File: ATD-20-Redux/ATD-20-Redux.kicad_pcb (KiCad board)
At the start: 2 copper layers, 17.8 x 57 mm, 5 parts, among them J1 RTC Pins, U1 DS1315, Y1 32.768 KHz

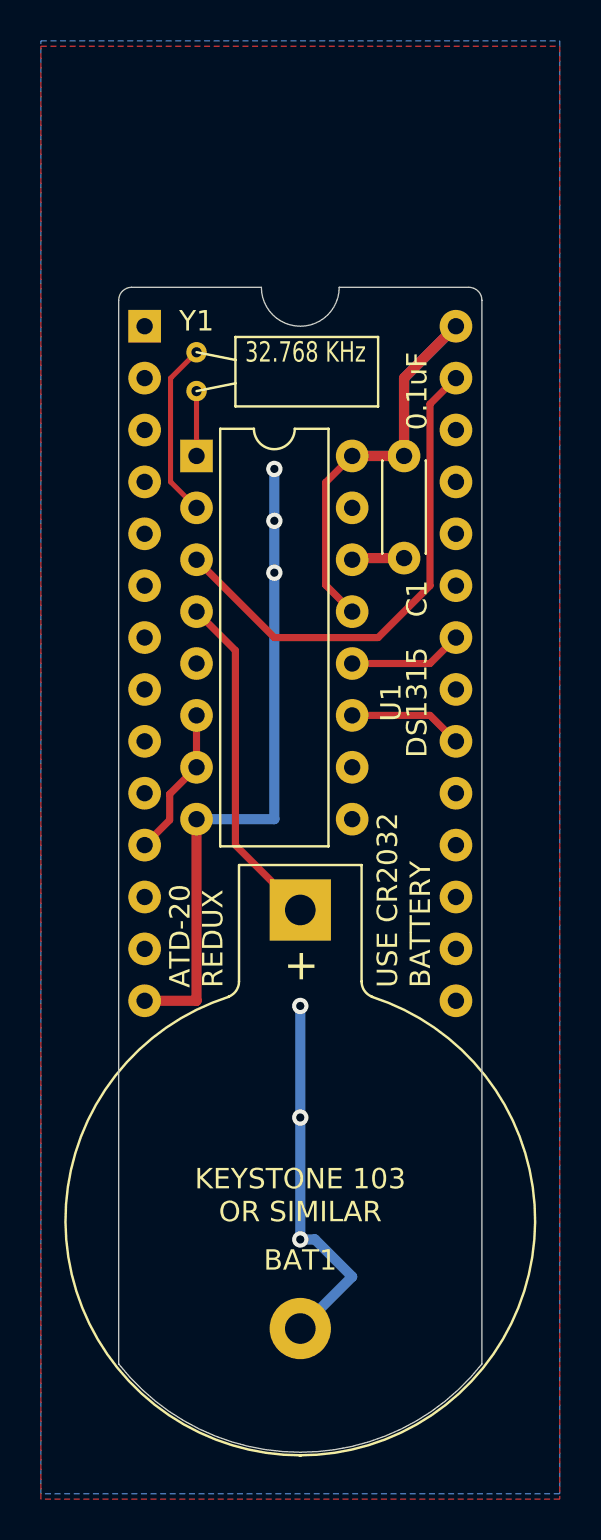
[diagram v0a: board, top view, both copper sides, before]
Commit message: Refinements to SmartWatchRedux and ATD-20-Redux after assembling initial run of boards.
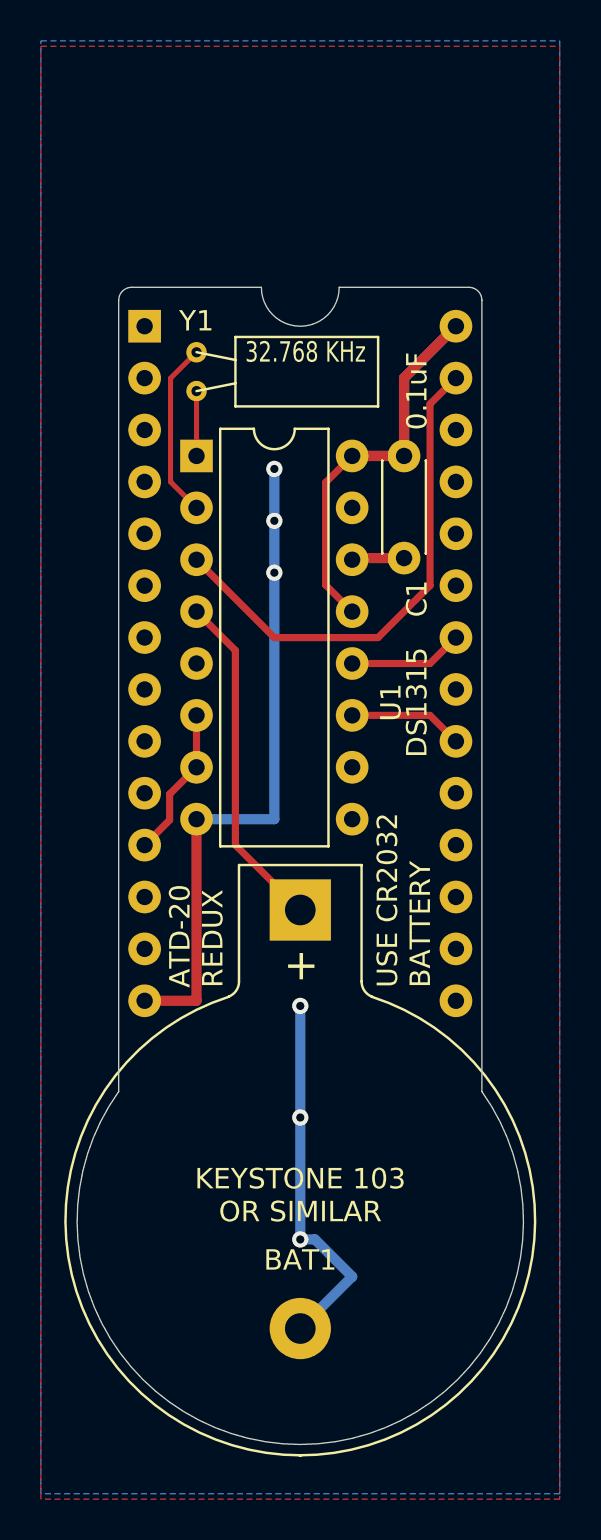
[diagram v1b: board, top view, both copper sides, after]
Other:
- board size 17.8 x 57 mm -> 21.8 x 56.6 mm

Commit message: Minor changes to ATD-20-Redux.
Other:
- board text added: "PIN 1"
